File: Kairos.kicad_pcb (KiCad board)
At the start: 2 copper layers, 285 x 94.6 mm, 134 parts, among them Q1 NSS40301MZ4T1G, U1 ATMEGA32U2-AU, Y1 Crystal_GND24

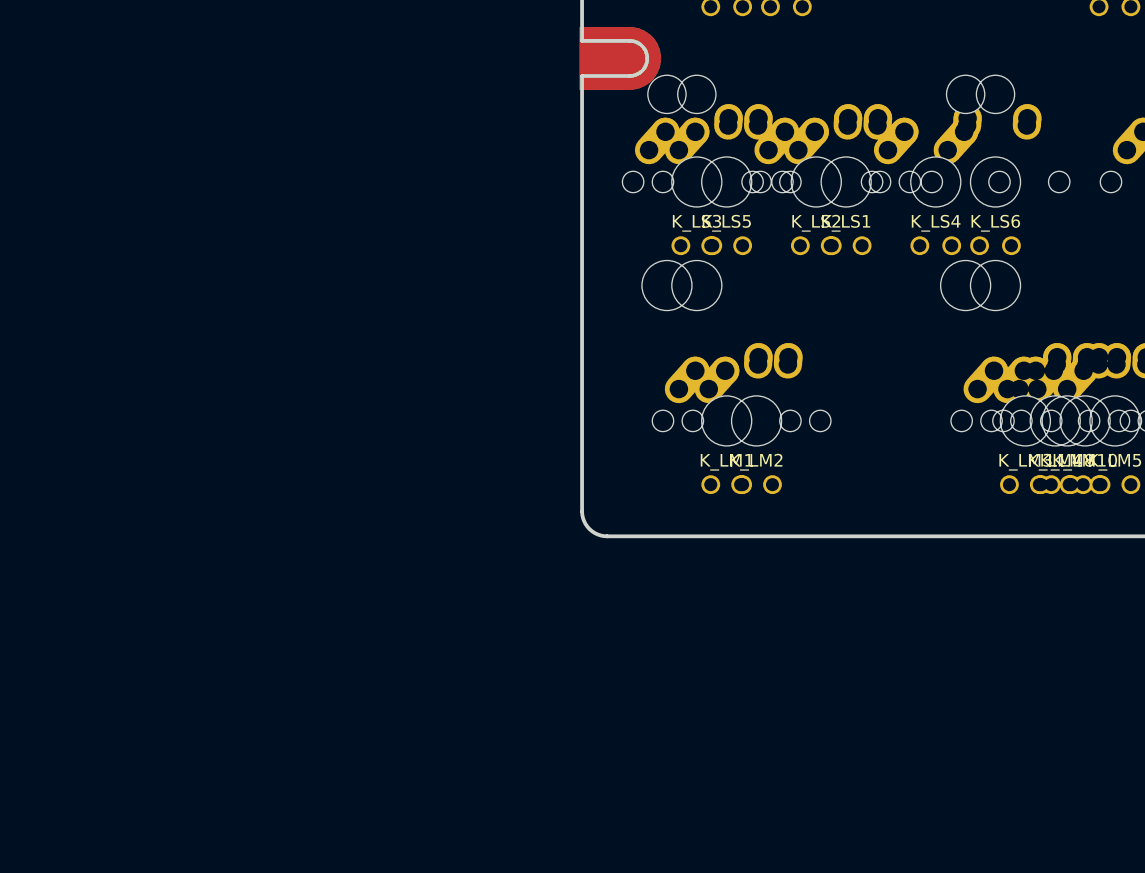
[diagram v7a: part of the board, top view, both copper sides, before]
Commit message: Breakout Left Shift to match diagram
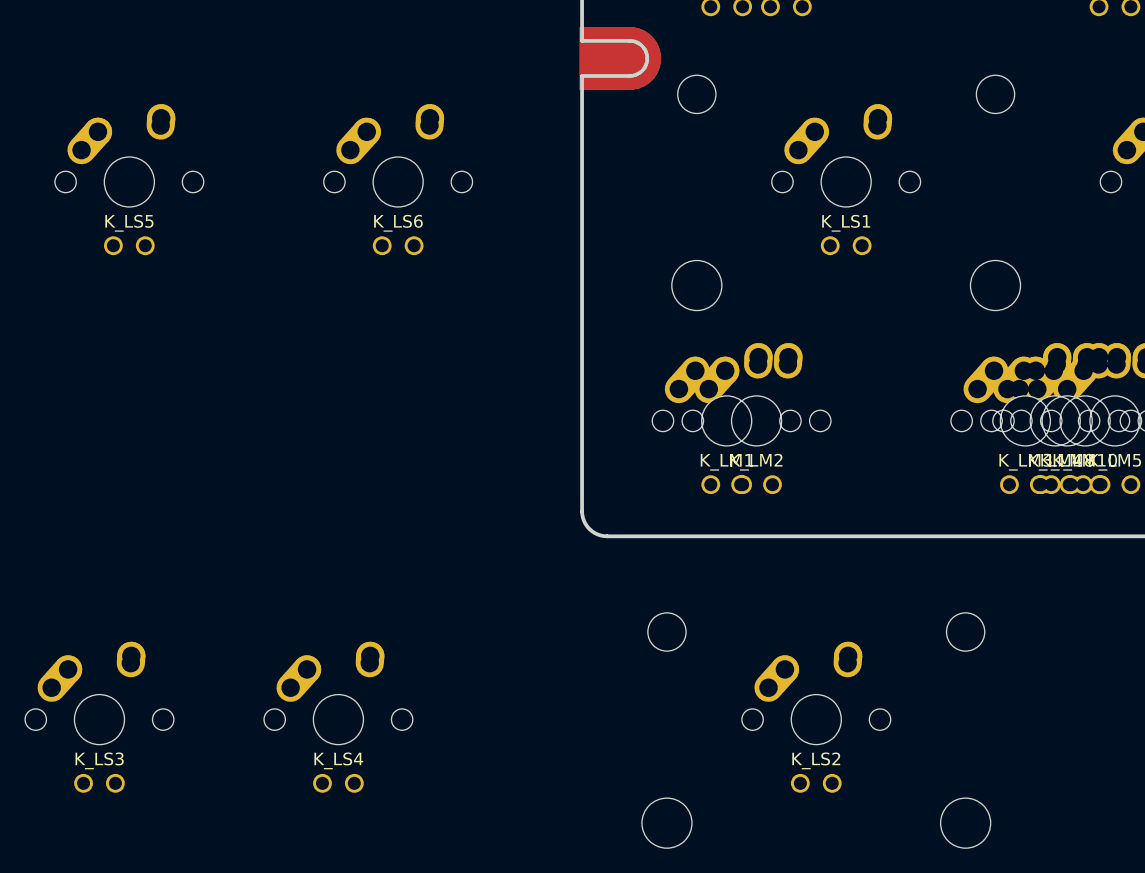
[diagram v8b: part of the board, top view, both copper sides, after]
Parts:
- moved K_LS3 64.1 mm to (-33.3, 131.0)
- moved K_LS4 64.1 mm to (-14.3, 131.0)
- moved K_LS5 47.6 mm to (-31.0, 88.1)
- moved K_LS6 47.6 mm to (-9.53, 88.1)
- moved K_LS2 42.9 mm to (23.8, 131.0)
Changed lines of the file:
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@@
     (pad_to_mask_clearance 0.2)
     (aux_axis_origin 0 0)
-    (visible_elements 7FFFFFFF)
+    (visible_elements 7FFFF7FF)
     (pcbplotparams
       (layerselection 0x00030_80000001)
@@
   )
   (module MX_Alps_Hybrid:MX-2U (layer F.Cu)
-    (at 23.8125 88.10625)
+    (at 23.8125 130.96875)
     (fp_text reference K_LS2 (at 0 3.175) (layer F.SilkS)
       (effects (font (size 1 1) (thickness 0.15)))
@@
   )
   (module MX_Alps_Hybrid:MX-1U (layer F.Cu)
-    (at 14.2875 88.10625)
+    (at -33.3375 130.96875)
     (fp_text reference K_LS3 (at 0 3.175) (layer F.SilkS)
       (effects (font (size 1 1) (thickness 0.15)))
@@
   )
   (module MX_Alps_Hybrid:MX-1U (layer F.Cu)
-    (at 33.3375 88.10625)
+    (at -14.2875 130.96875)
     (fp_text reference K_LS4 (at 0 3.175) (layer F.SilkS)
       (effects (font (size 1 1) (thickness 0.15)))
@@
   )
   (module MX_Alps_Hybrid:MX-1.25U (layer F.Cu)
-    (at 16.66875 88.10625)
+    (at -30.95625 88.10625)
     (fp_text reference K_LS5 (at 0 3.175) (layer F.SilkS)
       (effects (font (size 1 1) (thickness 0.15)))
@@
   )
   (module MX_Alps_Hybrid:MX-1U (layer F.Cu)
-    (at 38.1 88.10625)
+    (at -9.525 88.10625)
     (fp_text reference K_LS6 (at 0 3.175) (layer F.SilkS)
       (effects (font (size 1 1) (thickness 0.15)))
